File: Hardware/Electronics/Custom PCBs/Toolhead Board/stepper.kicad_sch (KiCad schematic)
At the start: 12 parts, among them U6 TMC2209-LA

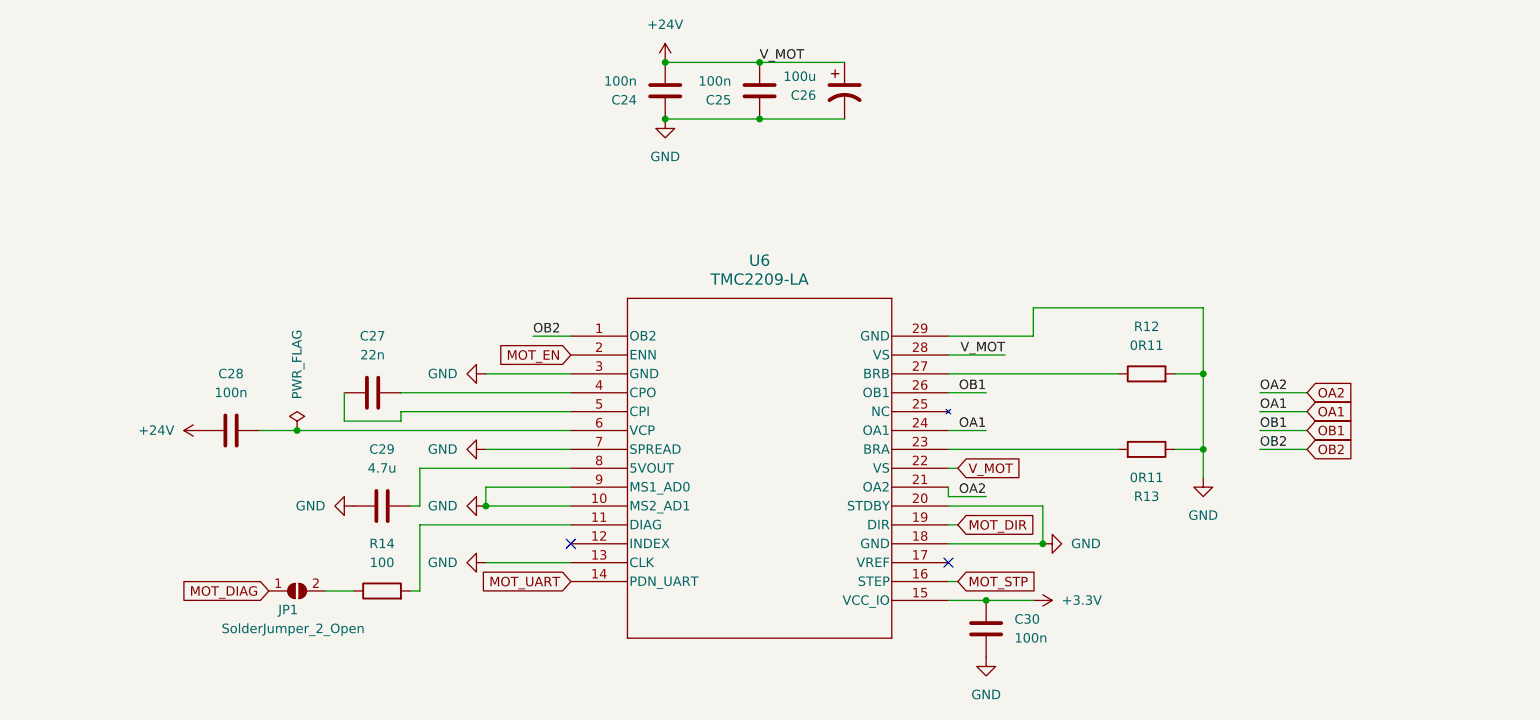
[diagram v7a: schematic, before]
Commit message: Update toolhead schematic+layout and add tolerances to base
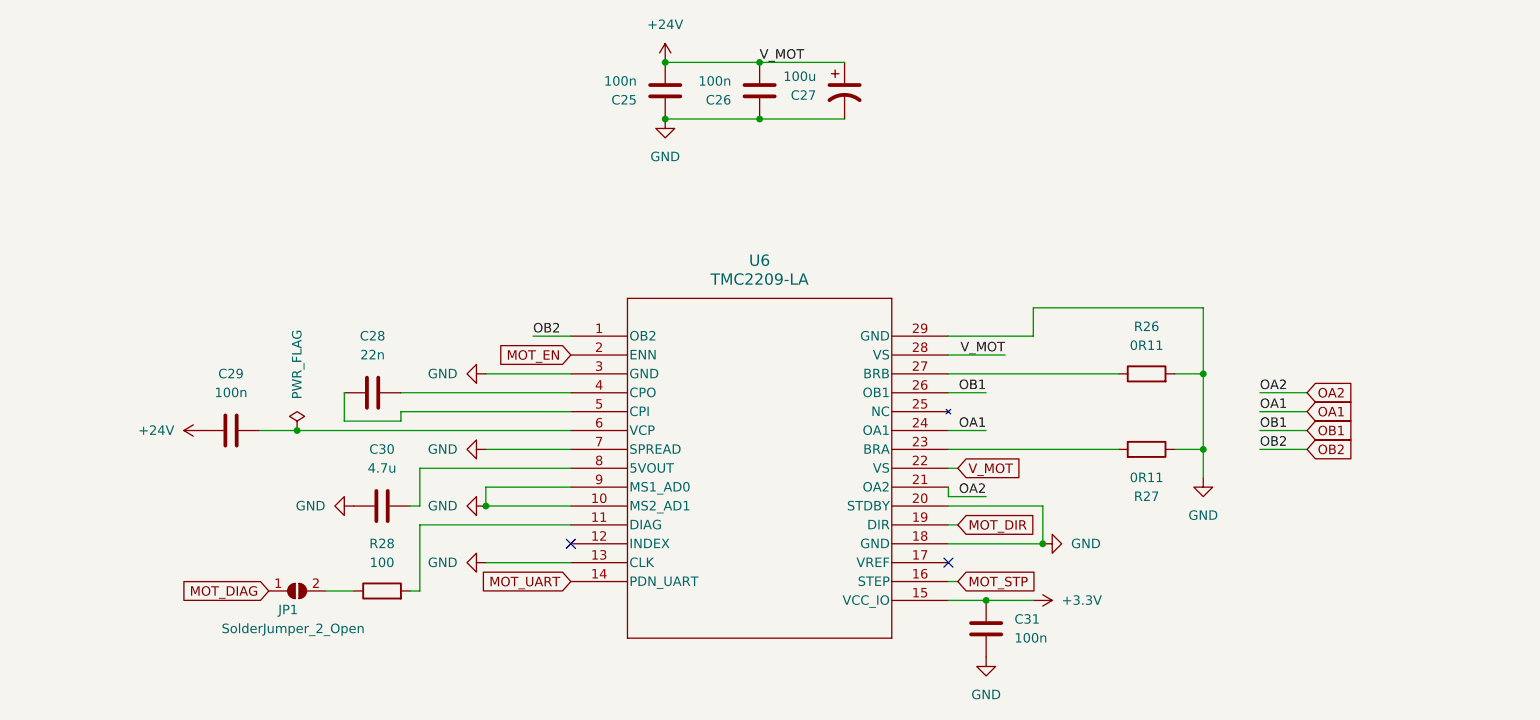
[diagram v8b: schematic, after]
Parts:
- renumbered C24 to C25, C25 to C26, C26 to C27, C27 to C28, C28 to C29, C29 to C30, C30 to C31, R12 to R26, R13 to R27, R14 to R28
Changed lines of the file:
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@@
 		(dnp no)
 		(fields_autoplaced yes)
-		(property "Reference" "#PWR062"
+		(property "Reference" "#PWR066"
 			(at 163.83 88.9 0)
 			(effects
@@
 			(project "Toolhead Board"
 				(path "/a1747683-152e-4245-ab61-2d33ce6021ef/1af119c3-7c67-4253-a987-5e4038b04e95"
-					(reference "#PWR062")
+					(reference "#PWR066")
 					(unit 1)
 				)
@@
 		(dnp no)
 		(fields_autoplaced yes)
-		(property "Reference" "C25"
+		(property "Reference" "C26"
 			(at 115.57 29.21 0)
 			(effects
@@
 			(project "Toolhead Board"
 				(path "/a1747683-152e-4245-ab61-2d33ce6021ef/1af119c3-7c67-4253-a987-5e4038b04e95"
-					(reference "C25")
+					(reference "C26")
 					(unit 1)
 				)
@@
 		(on_board yes)
 		(dnp no)
-		(property "Reference" "#FLG04"
+		(property "Reference" "#FLG05"
 			(at 57.15 71.755 0)
 			(effects
@@
 			(project "Toolhead Board"
 				(path "/a1747683-152e-4245-ab61-2d33ce6021ef/1af119c3-7c67-4253-a987-5e4038b04e95"
-					(reference "#FLG04")
+					(reference "#FLG05")
 					(unit 1)
 				)
@@
 		(dnp no)
 		(fields_autoplaced yes)
-		(property "Reference" "C28"
+		(property "Reference" "C29"
 			(at 48.26 66.04 90)
 			(effects
@@
 			(project "Toolhead Board"
 				(path "/a1747683-152e-4245-ab61-2d33ce6021ef/1af119c3-7c67-4253-a987-5e4038b04e95"
-					(reference "C28")
+					(reference "C29")
 					(unit 1)
 				)
@@
 		(dnp no)
 		(fields_autoplaced yes)
-		(property "Reference" "C30"
+		(property "Reference" "C31"
 			(at 153.67 99.06 0)
 			(effects
@@
 			(project "Toolhead Board"
 				(path "/a1747683-152e-4245-ab61-2d33ce6021ef/1af119c3-7c67-4253-a987-5e4038b04e95"
-					(reference "C30")
+					(reference "C31")
 					(unit 1)
 				)
@@
 		(dnp no)
 		(fields_autoplaced yes)
-		(property "Reference" "C26"
+		(property "Reference" "C27"
 			(at 127 28.575 0)
 			(effects
@@
 			(project "Toolhead Board"
 				(path "/a1747683-152e-4245-ab61-2d33ce6021ef/1af119c3-7c67-4253-a987-5e4038b04e95"
-					(reference "C26")
+					(reference "C27")
 					(unit 1)
 				)
@@
 		(dnp no)
 		(fields_autoplaced yes)
-		(property "Reference" "#PWR057"
+		(property "Reference" "#PWR061"
 			(at 48.26 73.66 0)
 			(effects
@@
 			(project "Toolhead Board"
 				(path "/a1747683-152e-4245-ab61-2d33ce6021ef/1af119c3-7c67-4253-a987-5e4038b04e95"
-					(reference "#PWR057")
+					(reference "#PWR061")
 					(unit 1)
 				)
@@
 		(dnp no)
 		(fields_autoplaced yes)
-		(property "Reference" "R12"
+		(property "Reference" "R26"
 			(at 171.45 59.69 90)
 			(effects
@@
 			(project "Toolhead Board"
 				(path "/a1747683-152e-4245-ab61-2d33ce6021ef/1af119c3-7c67-4253-a987-5e4038b04e95"
-					(reference "R12")
+					(reference "R26")
 					(unit 1)
 				)
@@
 		(dnp no)
 		(fields_autoplaced yes)
-		(property "Reference" "#PWR055"
+		(property "Reference" "#PWR059"
 			(at 106.68 38.1 0)
 			(effects
@@
 			(project "Toolhead Board"
 				(path "/a1747683-152e-4245-ab61-2d33ce6021ef/1af119c3-7c67-4253-a987-5e4038b04e95"
-					(reference "#PWR055")
+					(reference "#PWR059")
 					(unit 1)
 				)
@@
 		(dnp no)
 		(fields_autoplaced yes)
-		(property "Reference" "C29"
+		(property "Reference" "C30"
 			(at 68.58 76.2 90)
 			(effects
@@
 			(project "Toolhead Board"
 				(path "/a1747683-152e-4245-ab61-2d33ce6021ef/1af119c3-7c67-4253-a987-5e4038b04e95"
-					(reference "C29")
+					(reference "C30")
 					(unit 1)
 				)
@@
 		(dnp no)
 		(fields_autoplaced yes)
-		(property "Reference" "C27"
+		(property "Reference" "C28"
 			(at 67.31 60.96 90)
 			(effects
@@
 			(project "Toolhead Board"
 				(path "/a1747683-152e-4245-ab61-2d33ce6021ef/1af119c3-7c67-4253-a987-5e4038b04e95"
-					(reference "C27")
+					(reference "C28")
 					(unit 1)
 				)
@@
 		(dnp no)
 		(fields_autoplaced yes)
-		(property "Reference" "#PWR058"
+		(property "Reference" "#PWR062"
 			(at 76.2 76.2 0)
 			(effects
@@
 			(project "Toolhead Board"
 				(path "/a1747683-152e-4245-ab61-2d33ce6021ef/1af119c3-7c67-4253-a987-5e4038b04e95"
-					(reference "#PWR058")
+					(reference "#PWR062")
 					(unit 1)
 				)
@@
 		(dnp no)
 		(fields_autoplaced yes)
-		(property "Reference" "#PWR059"
+		(property "Reference" "#PWR063"
 			(at 179.07 86.36 0)
 			(effects
@@
 			(project "Toolhead Board"
 				(path "/a1747683-152e-4245-ab61-2d33ce6021ef/1af119c3-7c67-4253-a987-5e4038b04e95"
-					(reference "#PWR059")
+					(reference "#PWR063")
 					(unit 1)
 				)
@@
 		(dnp no)
 		(fields_autoplaced yes)
-		(property "Reference" "#PWR056"
+		(property "Reference" "#PWR060"
 			(at 76.2 66.04 0)
 			(effects
@@
 			(project "Toolhead Board"
 				(path "/a1747683-152e-4245-ab61-2d33ce6021ef/1af119c3-7c67-4253-a987-5e4038b04e95"
-					(reference "#PWR056")
+					(reference "#PWR060")
 					(unit 1)
 				)
@@
 		(dnp no)
 		(fields_autoplaced yes)
-		(property "Reference" "#PWR054"
+		(property "Reference" "#PWR058"
 			(at 106.68 27.94 0)
 			(effects
@@
 			(project "Toolhead Board"
 				(path "/a1747683-152e-4245-ab61-2d33ce6021ef/1af119c3-7c67-4253-a987-5e4038b04e95"
-					(reference "#PWR054")
+					(reference "#PWR058")
 					(unit 1)
 				)
@@
 		(dnp no)
 		(fields_autoplaced yes)
-		(property "Reference" "#PWR065"
+		(property "Reference" "#PWR069"
 			(at 149.86 110.49 0)
 			(effects
@@
 			(project "Toolhead Board"
 				(path "/a1747683-152e-4245-ab61-2d33ce6021ef/1af119c3-7c67-4253-a987-5e4038b04e95"
-					(reference "#PWR065")
+					(reference "#PWR069")
 					(unit 1)
 				)
@@
 		(dnp no)
 		(fields_autoplaced yes)
-		(property "Reference" "R14"
+		(property "Reference" "R28"
 			(at 68.58 88.9 90)
 			(effects
@@
 			(project "Toolhead Board"
 				(path "/a1747683-152e-4245-ab61-2d33ce6021ef/1af119c3-7c67-4253-a987-5e4038b04e95"
-					(reference "R14")
+					(reference "R28")
 					(unit 1)
 				)
@@
 		(dnp no)
 		(fields_autoplaced yes)
-		(property "Reference" "C24"
+		(property "Reference" "C25"
 			(at 102.87 29.21 0)
 			(effects
@@
 			(project "Toolhead Board"
 				(path "/a1747683-152e-4245-ab61-2d33ce6021ef/1af119c3-7c67-4253-a987-5e4038b04e95"
-					(reference "C24")
+					(reference "C25")
 					(unit 1)
 				)
@@
 		(dnp no)
 		(fields_autoplaced yes)
-		(property "Reference" "#PWR063"
+		(property "Reference" "#PWR067"
 			(at 76.2 91.44 0)
 			(effects
@@
 			(project "Toolhead Board"
 				(path "/a1747683-152e-4245-ab61-2d33ce6021ef/1af119c3-7c67-4253-a987-5e4038b04e95"
-					(reference "#PWR063")
+					(reference "#PWR067")
 					(unit 1)
 				)
@@
 		(dnp no)
 		(fields_autoplaced yes)
-		(property "Reference" "#PWR060"
+		(property "Reference" "#PWR064"
 			(at 58.42 83.82 0)
 			(effects
@@
 			(project "Toolhead Board"
 				(path "/a1747683-152e-4245-ab61-2d33ce6021ef/1af119c3-7c67-4253-a987-5e4038b04e95"
-					(reference "#PWR060")
+					(reference "#PWR064")
 					(unit 1)
 				)
@@
 		(on_board yes)
 		(dnp no)
-		(property "Reference" "R13"
+		(property "Reference" "R27"
 			(at 171.45 82.55 90)
 			(effects
@@
 			(project "Toolhead Board"
 				(path "/a1747683-152e-4245-ab61-2d33ce6021ef/1af119c3-7c67-4253-a987-5e4038b04e95"
-					(reference "R13")
+					(reference "R27")
 					(unit 1)
 				)
@@
 		(dnp no)
 		(fields_autoplaced yes)
-		(property "Reference" "#PWR064"
+		(property "Reference" "#PWR068"
 			(at 152.4 96.52 0)
 			(effects
@@
 			(project "Toolhead Board"
 				(path "/a1747683-152e-4245-ab61-2d33ce6021ef/1af119c3-7c67-4253-a987-5e4038b04e95"
-					(reference "#PWR064")
+					(reference "#PWR068")
 					(unit 1)
 				)
@@
 		(dnp no)
 		(fields_autoplaced yes)
-		(property "Reference" "#PWR061"
+		(property "Reference" "#PWR065"
 			(at 76.2 83.82 0)
 			(effects
@@
 			(project "Toolhead Board"
 				(path "/a1747683-152e-4245-ab61-2d33ce6021ef/1af119c3-7c67-4253-a987-5e4038b04e95"
-					(reference "#PWR061")
-					(unit 1)
-				)
+					(reference "#PWR065")
+					(unit 1)
+				)
